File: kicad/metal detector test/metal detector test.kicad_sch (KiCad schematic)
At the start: 108 parts, among them J1 3.5mm audio jack TRS, Q1 PNP, Q2 NPN, SW0 SW_SPST, SW1 SW_SPST, SW10 SW_SPST, SW2 SW_SPST, SW3 SW_SPST, SW4 SW_SPST, SW5 SW_SPST, SW6 SW_SPST, SW7 SW_SPST, SW8 SW_SPST, U1 op amp (higher voltage), U10 3.3v lin reg, U11 lp filter, U12 op amp (lower voltage), U2 nucleo-32 uC module, U3 9v lin reg, U4 5v lin reg, U5 3.3v lin reg, U6 audio amp, U7 lp filter, U8 switch debounce, U9 5v lin reg

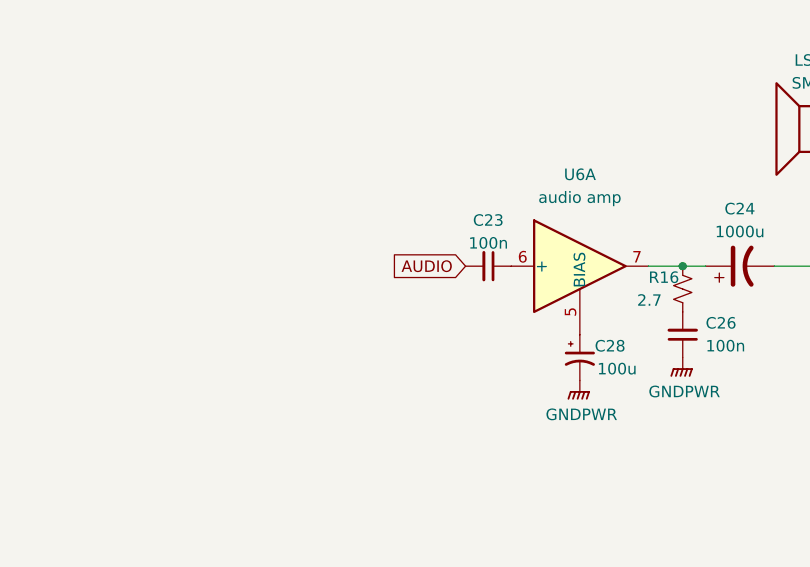
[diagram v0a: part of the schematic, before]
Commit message: considering filtering the audio output
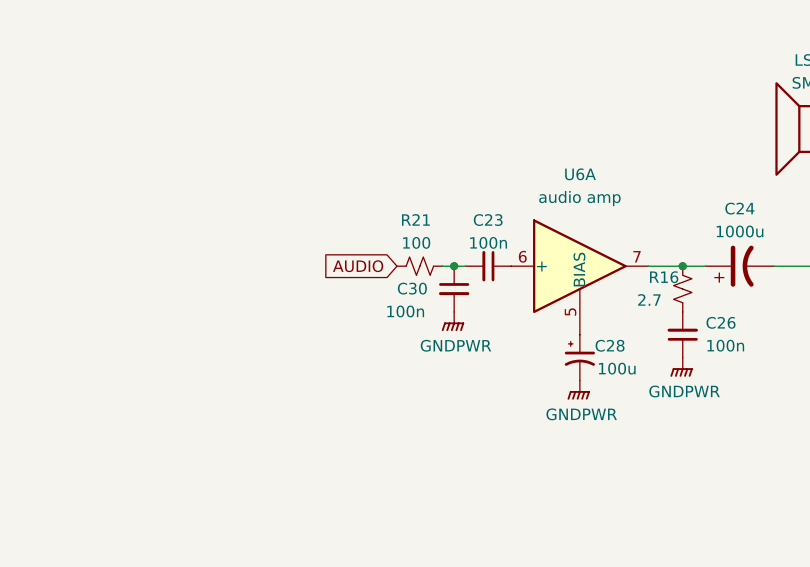
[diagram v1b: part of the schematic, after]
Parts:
- added C30: 100n, Capacitor_SMD:C_0805_2012Metric_Pad1.18x1.45mm_HandSolder, symbol Device:C_Small
- added R21: 100, Resistor_SMD:R_0805_2012Metric_Pad1.20x1.40mm_HandSolder, symbol Device:R_Small_US
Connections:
- net AUDIO: now also R21.1; no longer C23.2
- net GNDA: now also C30.2
- new net: C23.2, C30.1, R21.2
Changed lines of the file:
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@@
   (junction (at 27.94 81.28) (diameter 0) (color 0 0 0 0)
   )
+  (junction (at 207.01 148.59) (diameter 0) (color 0 0 0 0)
+  )
   (junction (at 46.99 177.8) (diameter 0) (color 0 0 0 0)
   )
@@
     (stroke (width 0) (type default))
   )
+  (wire (pts (xy 205.74 148.59) (xy 207.01 148.59))
+    (stroke (width 0) (type default))
+  )
   (wire (pts (xy 100.33 46.99) (xy 96.52 46.99))
     (stroke (width 0) (type default))
@@
     (stroke (width 0) (type default))
   )
+  (wire (pts (xy 207.01 148.59) (xy 208.28 148.59))
+    (stroke (width 0) (type default))
+  )
   (wire (pts (xy 46.99 147.32) (xy 41.91 147.32))
     (stroke (width 0) (type default))
@@
     )
   )
-  (global_label "AUDIO" (shape input) (at 208.28 148.59 180) (fields_autoplaced)
+  (global_label "AUDIO" (shape input) (at 200.66 148.59 180) (fields_autoplaced)
     (effects (font (size 1.27 1.27)) (justify right))
-    (property "Intersheetrefs" "${INTERSHEET_REFS}" (at 200.2426 148.5106 0)
+    (property "Intersheetrefs" "${INTERSHEET_REFS}" (at 192.6226 148.5106 0)
       (effects (font (size 1.27 1.27)) (justify right) hide)
     )
@@
     )
   )
+  (symbol (lib_id "Device:R_Small_US") (at 203.2 148.59 90) (unit 1)
+    (in_bom yes) (on_board yes) (dnp no)
+    (property "Reference" "R21" (at 204.47 143.51 90)
+      (effects (font (size 1.27 1.27)) (justify left))
+    )
+    (property "Value" "100" (at 204.47 146.05 90)
+      (effects (font (size 1.27 1.27)) (justify left))
+    )
+    (property "Footprint" "Resistor_SMD:R_0805_2012Metric_Pad1.20x1.40mm_HandSolder" (at 203.2 148.59 0)
+      (effects (font (size 1.27 1.27)) hide)
+    )
+    (property "Datasheet" "~" (at 203.2 148.59 0)
+      (effects (font (size 1.27 1.27)) hide)
+    )
+    (pin "1")
+    (pin "2")
+    (instances
+      (project "metal detector test"
+        (path "/aac94249-970f-41d5-8c24-6bade512464d"
+          (reference "R21") (unit 1)
+        )
+      )
+    )
+  )
   (symbol (lib_id "allen_opamp:OPA2320AID") (at 35.56 177.8 0) (unit 2)
     (in_bom yes) (on_board yes) (dnp no)
@@
     )
   )
+  (symbol (lib_id "Device:C_Small") (at 207.01 151.13 0) (unit 1)
+    (in_bom yes) (on_board yes) (dnp no)
+    (property "Reference" "C30" (at 200.66 151.13 0)
+      (effects (font (size 1.27 1.27)) (justify left))
+    )
+    (property "Value" "100n" (at 199.39 153.67 0)
+      (effects (font (size 1.27 1.27)) (justify left))
+    )
+    (property "Footprint" "Capacitor_SMD:C_0805_2012Metric_Pad1.18x1.45mm_HandSolder" (at 207.01 151.13 0)
+      (effects (font (size 1.27 1.27)) hide)
+    )
+    (property "Datasheet" "~" (at 207.01 151.13 0)
+      (effects (font (size 1.27 1.27)) hide)
+    )
+    (pin "1")
+    (pin "2")
+    (instances
+      (project "metal detector test"
+        (path "/aac94249-970f-41d5-8c24-6bade512464d"
+          (reference "C30") (unit 1)
+        )
+      )
+    )
+  )
   (symbol (lib_id "Device:Speaker") (at 266.7 132.08 0) (unit 1)
     (in_bom yes) (on_board yes) (dnp no) (fields_autoplaced)
@@
         )
       )
+    )
+  )
+  (symbol (lib_id "power:GNDPWR") (at 207.01 153.67 0) (unit 1)
+    (in_bom yes) (on_board yes) (dnp no)
+    (property "Reference" "#PWR061" (at 207.01 158.75 0)
+      (effects (font (size 1.27 1.27)) hide)
+    )
+    (property "Value" "GNDPWR" (at 203.2 157.48 0)
+      (effects (font (size 1.27 1.27)) (justify left))
+    )
+    (property "Footprint" "" (at 207.01 154.94 0)
+      (effects (font (size 1.27 1.27)) hide)
+    )
+    (property "Datasheet" "" (at 207.01 154.94 0)
+      (effects (font (size 1.27 1.27)) hide)
+    )
+    (pin "1")
+    (instances
+      (project "metal detector test"
+        (path "/aac94249-970f-41d5-8c24-6bade512464d"
+          (reference "#PWR061") (unit 1)
+        )
+      )

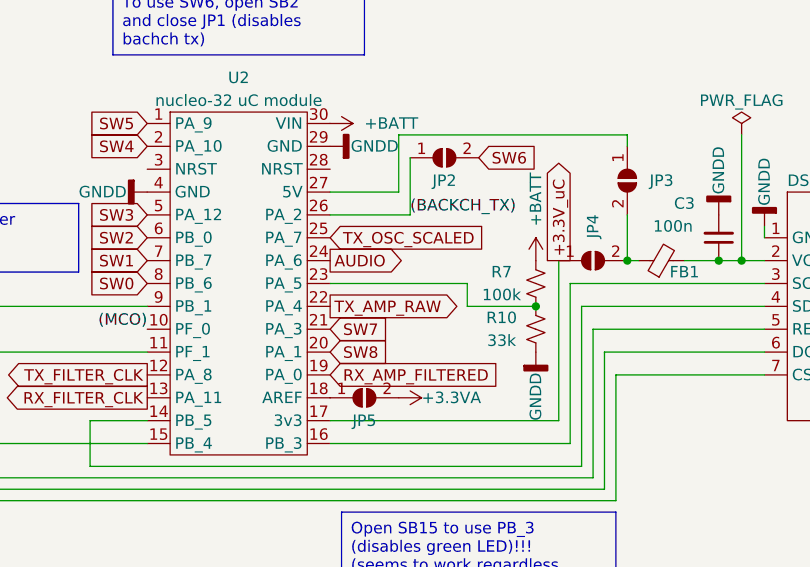
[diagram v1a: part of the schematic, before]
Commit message: Swapped DAC outputs for better impedance balancing
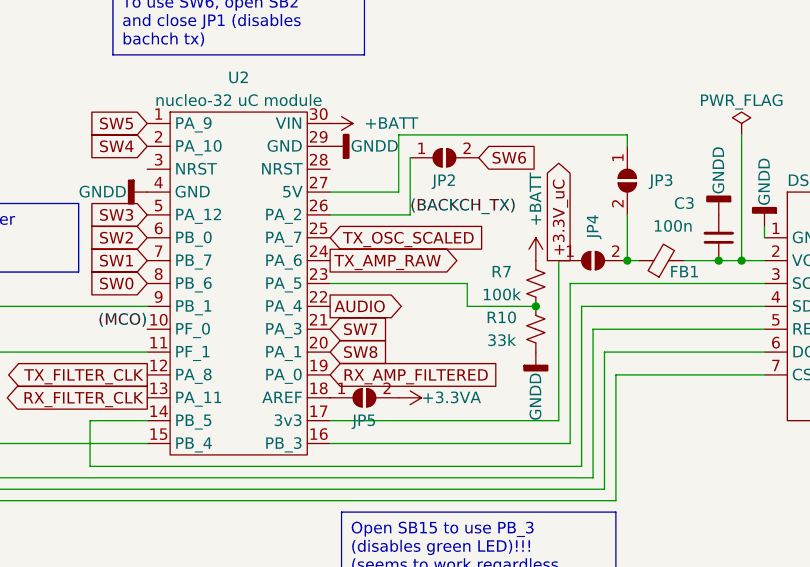
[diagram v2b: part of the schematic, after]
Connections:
- net AUDIO: now also U2.22 (PA_4); no longer U2.24 (PA_6)
- net TX_AMP_RAW: now also U2.24 (PA_6); no longer U2.22 (PA_4)
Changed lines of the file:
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@@
     )
   )
-  (global_label "AUDIO" (shape output) (at 217.17 43.18 0) (fields_autoplaced)
+  (global_label "AUDIO" (shape output) (at 217.17 48.26 0) (fields_autoplaced)
     (effects (font (size 1.27 1.27)) (justify left))
-    (property "Intersheetrefs" "${INTERSHEET_REFS}" (at 225.7002 43.18 0)
+    (property "Intersheetrefs" "${INTERSHEET_REFS}" (at 225.7002 48.26 0)
       (effects (font (size 1.27 1.27)) (justify left) hide)
     )
@@
     )
   )
-  (global_label "TX_AMP_RAW" (shape output) (at 217.17 48.26 0) (fields_autoplaced)
+  (global_label "TX_AMP_RAW" (shape output) (at 217.17 43.18 0) (fields_autoplaced)
     (effects (font (size 1.27 1.27)) (justify left))
-    (property "Intersheetrefs" "${INTERSHEET_REFS}" (at 231.8081 48.26 0)
+    (property "Intersheetrefs" "${INTERSHEET_REFS}" (at 231.8081 43.18 0)
       (effects (font (size 1.27 1.27)) (justify left) hide)
     )

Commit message: About halfway done routing tracks/traces
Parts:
- removed TP3: TX_D_AMP, TestPoint:TestPoint_Pad_D1.5mm, symbol Connector:TestPoint
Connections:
- net AUDIO: now also U2.24 (PA_6); no longer U2.22 (PA_4)
- net TX_AMP_RAW: now also U2.22 (PA_4); no longer U2.24 (PA_6)
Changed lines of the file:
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@@
   (junction (at 274.32 95.25) (diameter 0) (color 0 0 0 0)
-  )
-  (junction (at 205.74 97.79) (diameter 0) (color 0 0 0 0)
   )
   (junction (at 168.91 97.79) (diameter 0) (color 0 0 0 0)
@@
     )
   )
-  (global_label "AUDIO" (shape output) (at 217.17 48.26 0) (fields_autoplaced)
-    (effects (font (size 1.27 1.27)) (justify left))
-    (property "Intersheetrefs" "${INTERSHEET_REFS}" (at 225.7002 48.26 0)
+  (global_label "AUDIO" (shape output) (at 217.17 43.18 0) (fields_autoplaced)
+    (effects (font (size 1.27 1.27)) (justify left))
+    (property "Intersheetrefs" "${INTERSHEET_REFS}" (at 225.7002 43.18 0)
       (effects (font (size 1.27 1.27)) (justify left) hide)
     )
@@
     )
   )
-  (global_label "TX_AMP_RAW" (shape output) (at 217.17 43.18 0) (fields_autoplaced)
-    (effects (font (size 1.27 1.27)) (justify left))
-    (property "Intersheetrefs" "${INTERSHEET_REFS}" (at 231.8081 43.18 0)
+  (global_label "TX_AMP_RAW" (shape output) (at 217.17 48.26 0) (fields_autoplaced)
+    (effects (font (size 1.27 1.27)) (justify left))
+    (property "Intersheetrefs" "${INTERSHEET_REFS}" (at 231.8081 48.26 0)
       (effects (font (size 1.27 1.27)) (justify left) hide)
     )
@@
         )
       )
-    )
-  )
-  (symbol (lib_id "Connector:TestPoint") (at 205.74 97.79 0) (unit 1)
-    (in_bom yes) (on_board yes) (dnp no) (fields_autoplaced)
-    (property "Reference" "TP3" (at 208.28 93.853 0)
-      (effects (font (size 1.27 1.27)) (justify left))
-    )
-    (property "Value" "TX_D_AMP" (at 208.28 96.393 0)
-      (effects (font (size 1.27 1.27)) (justify left))
-    )
-    (property "Footprint" "TestPoint:TestPoint_Pad_D1.5mm" (at 210.82 97.79 0)
-      (effects (font (size 1.27 1.27)) hide)
-    )
-    (property "Datasheet" "~" (at 210.82 97.79 0)
-      (effects (font (size 1.27 1.27)) hide)
-    )
-    (property "MPN" "" (at 205.74 97.79 0)
-      (effects (font (size 1.27 1.27)) hide)
-    )
-    (pin "1")
-    (instances
-      (project "metal detector test"
-        (path "/aac94249-970f-41d5-8c24-6bade512464d"
-          (reference "TP3") (unit 1)
-        )
-      )

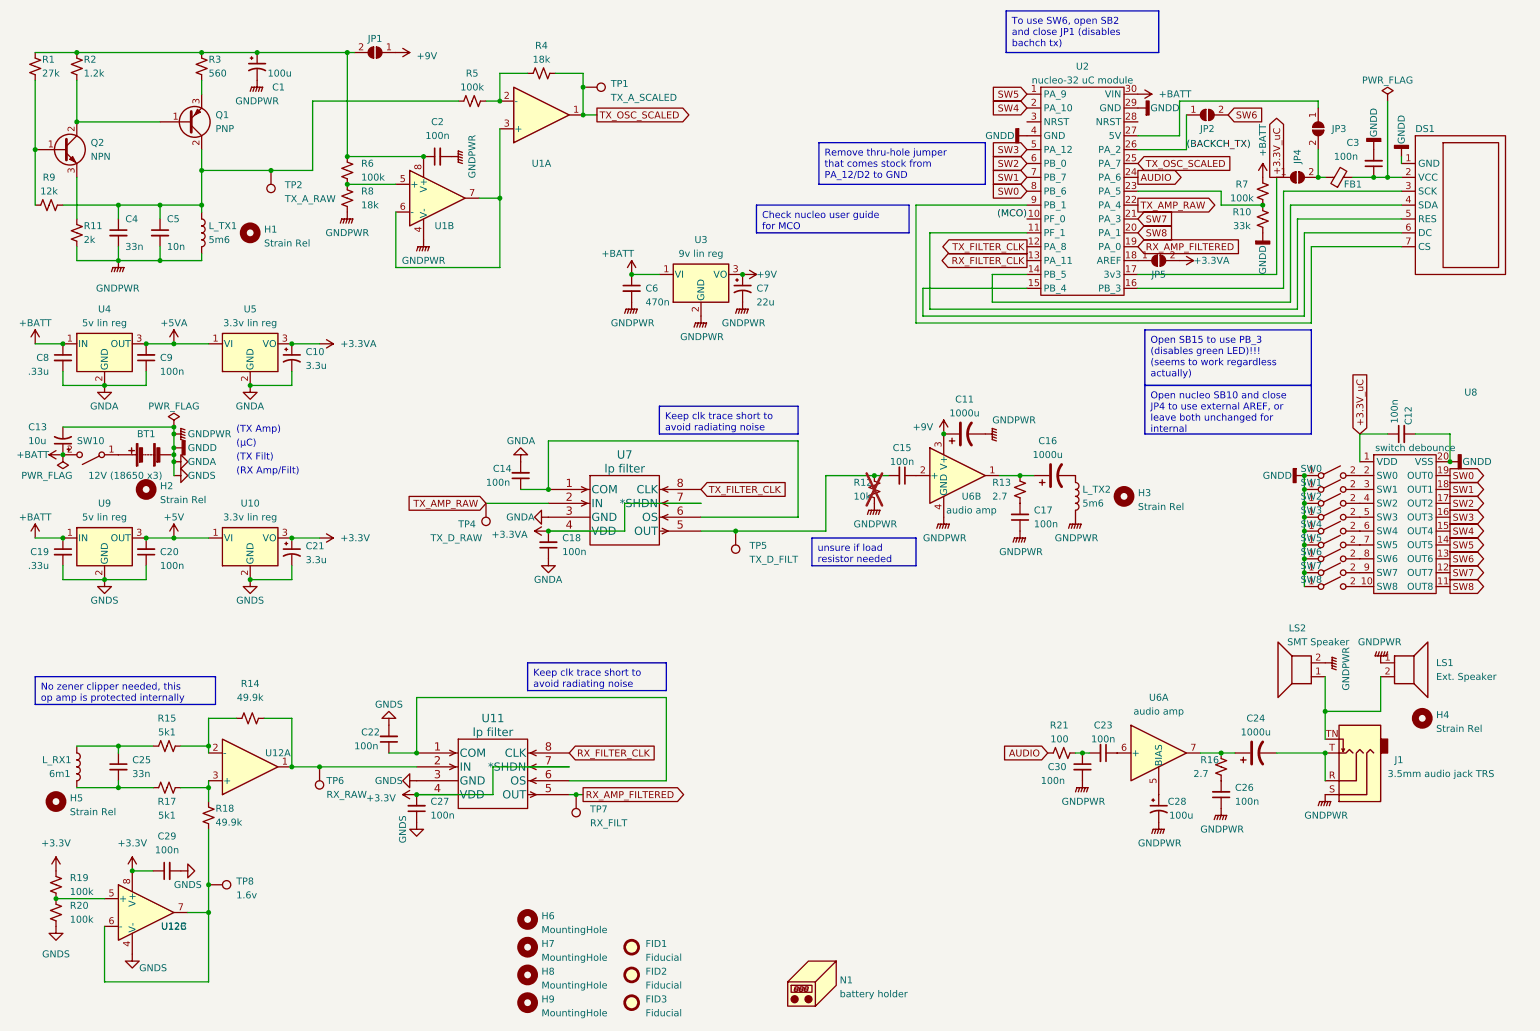
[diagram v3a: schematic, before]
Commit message: Everything but gnd should be routed
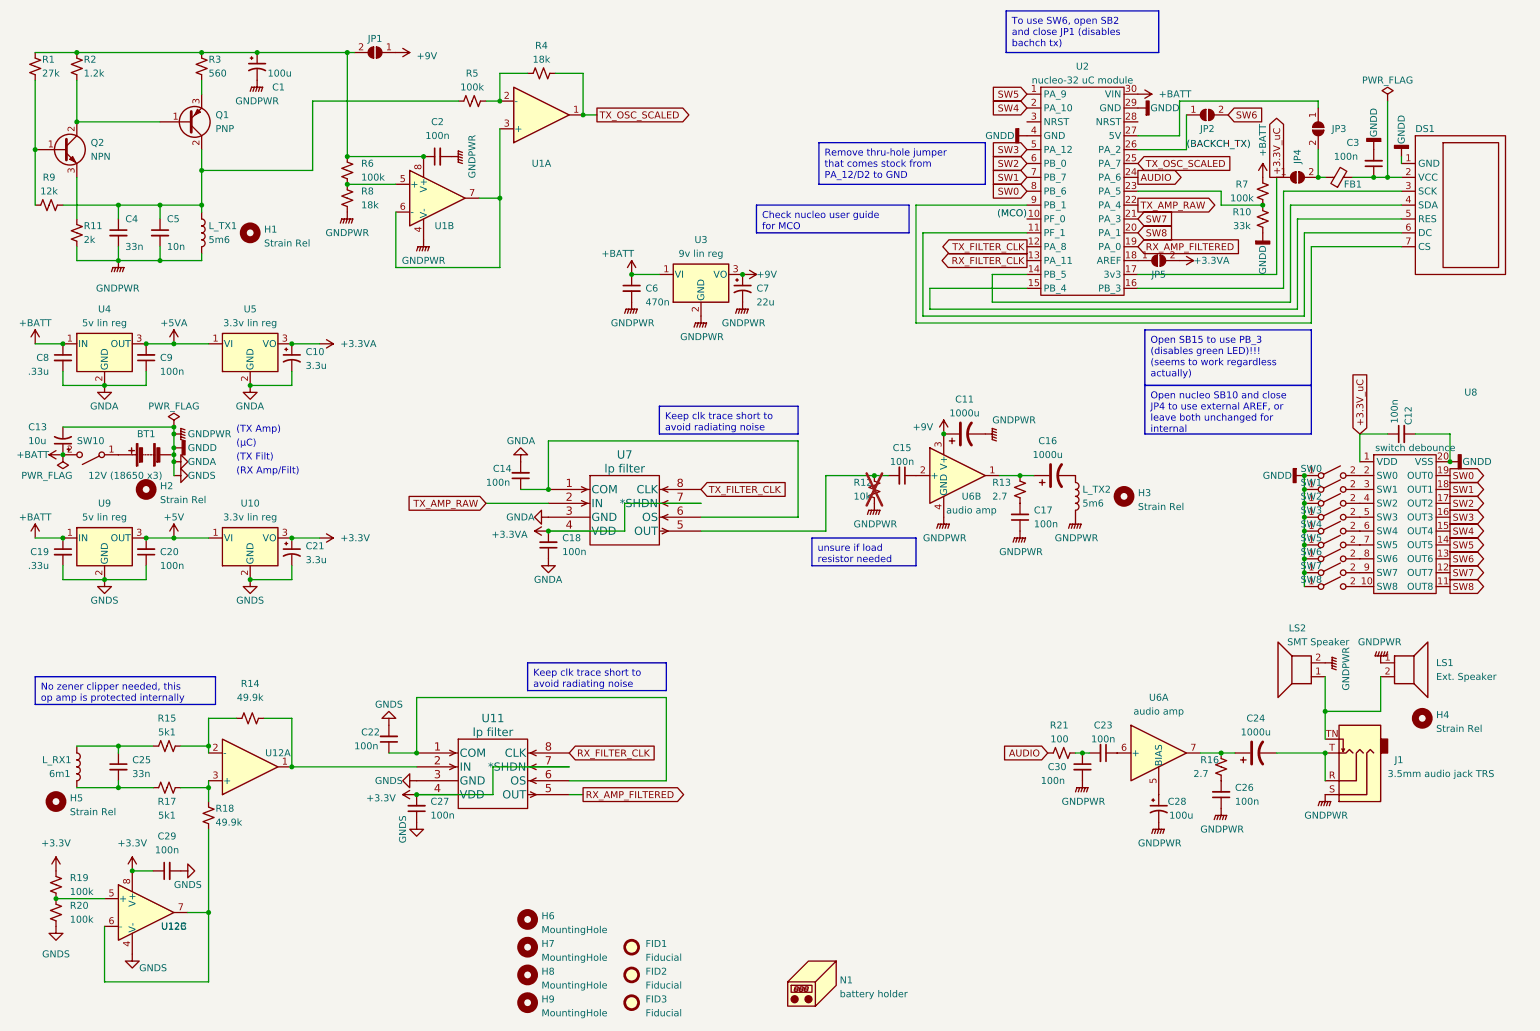
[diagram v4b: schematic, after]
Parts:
- removed TP1: TX_A_SCALED, TestPoint:TestPoint_Pad_D1.5mm, symbol Connector:TestPoint
- removed TP2: TX_A_RAW, TestPoint:TestPoint_Pad_D1.5mm, symbol Connector:TestPoint
- removed TP4: TX_D_RAW, TestPoint:TestPoint_Pad_D1.5mm, symbol Connector:TestPoint
- removed TP5: TX_D_FILT, TestPoint:TestPoint_Pad_D1.5mm, symbol Connector:TestPoint
- removed TP6: RX_RAW, TestPoint:TestPoint_Pad_D1.5mm, symbol Connector:TestPoint
- removed TP7: RX_FILT, TestPoint:TestPoint_Pad_D1.5mm, symbol Connector:TestPoint
- removed TP8: 1.6v, TestPoint:TestPoint_Pad_D1.5mm, symbol Connector:TestPoint
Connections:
- net at DS1.5 (RES): now also U2.15 (PB_4); no longer U2.11 (PF_1)
- net at DS1.6 (DC): now also U2.11 (PF_1); no longer U2.15 (PB_4)
